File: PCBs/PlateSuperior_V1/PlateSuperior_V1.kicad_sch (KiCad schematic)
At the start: 48 parts, among them J1 Conn_01x04, J2 Conn_01x04, J3 Conn_02x10_Counter_Clockwise, SW1 SW_Push, SW10 SW_Push, SW11 SW_Push, SW12 SW_Push, SW13 SW_Push, SW14 SW_Push, SW15 SW_Push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

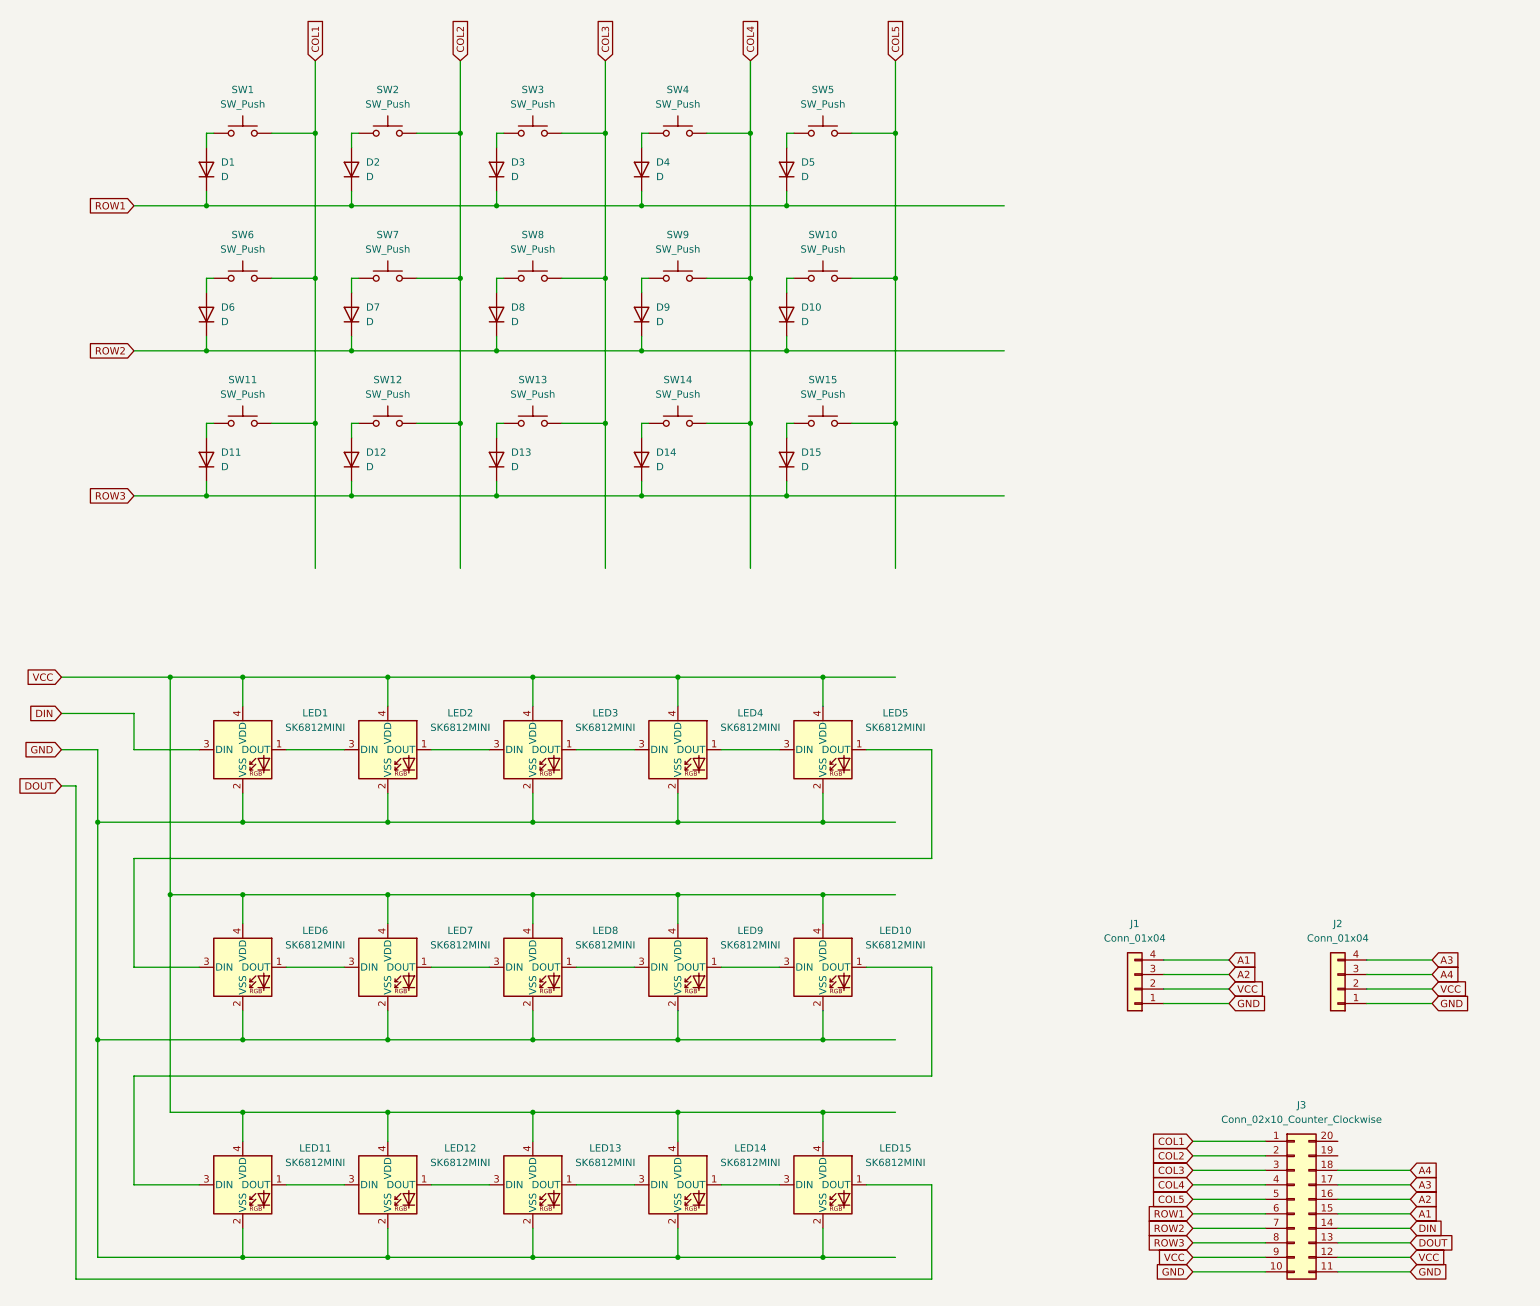
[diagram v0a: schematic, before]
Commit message: Add plates
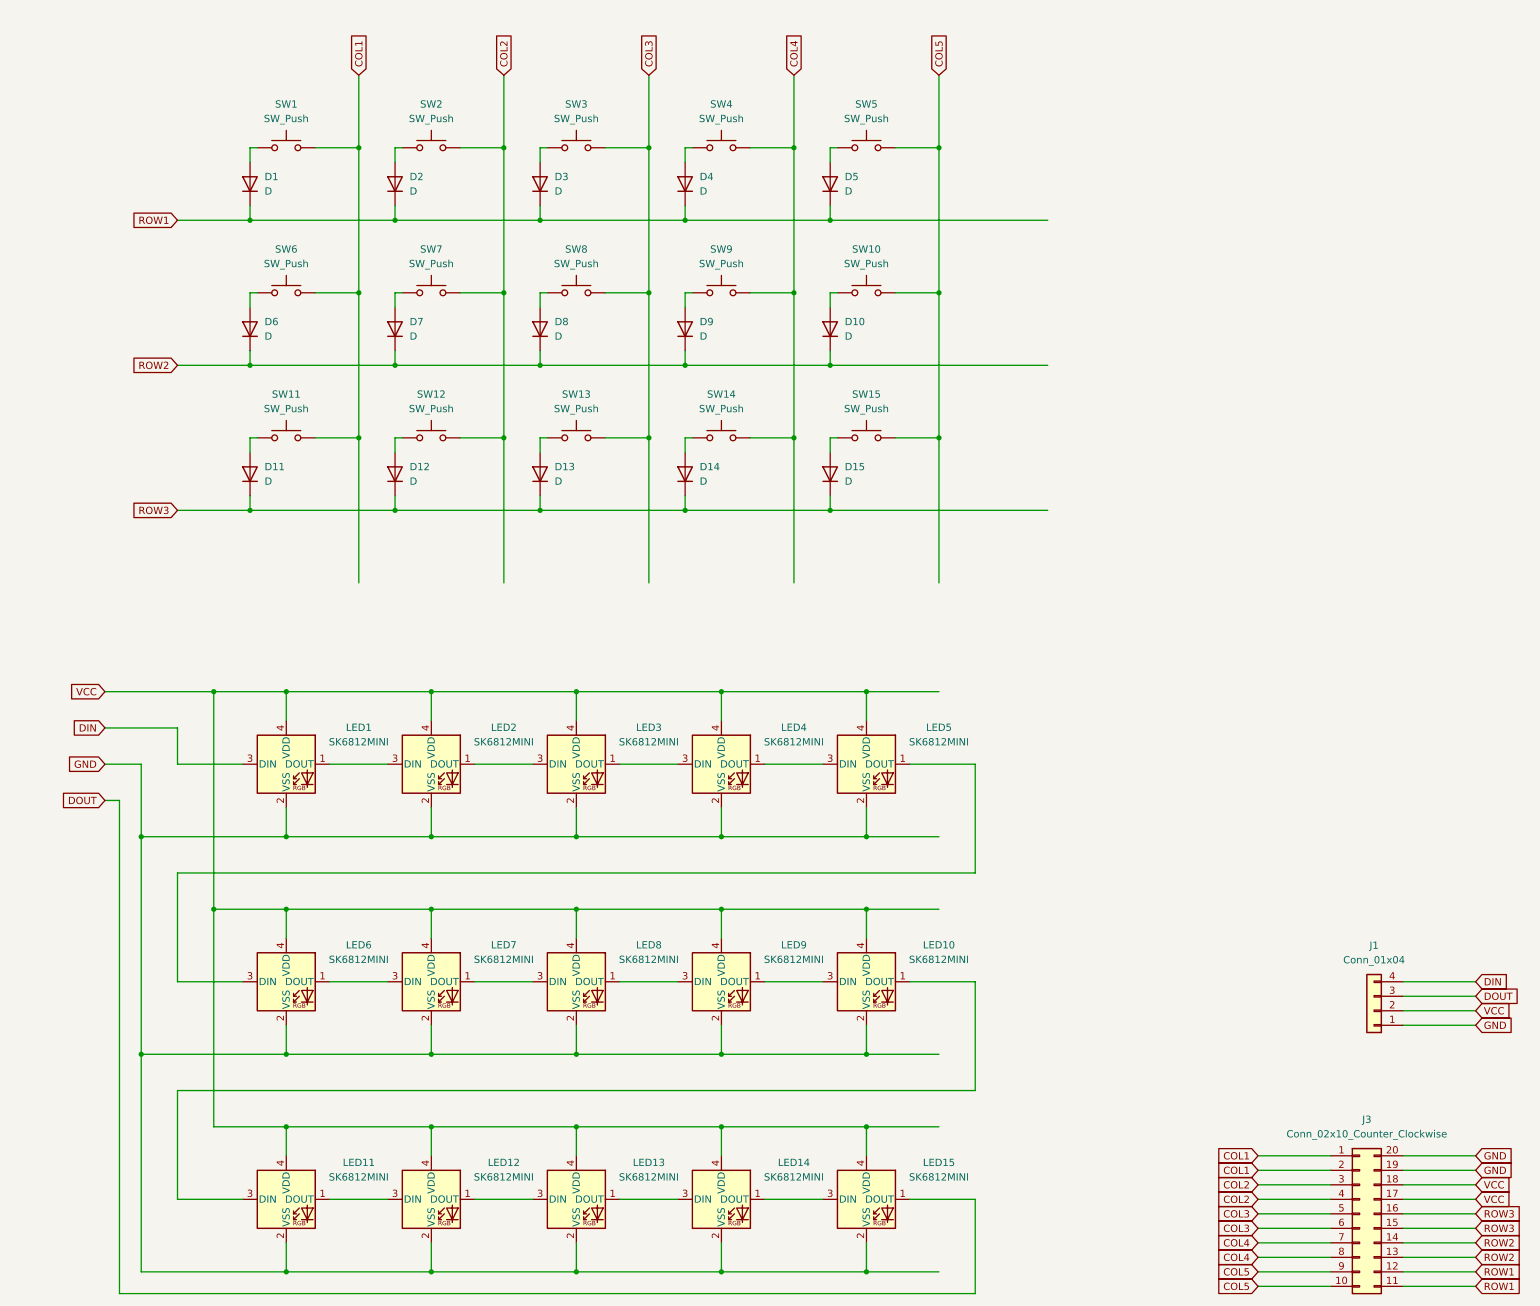
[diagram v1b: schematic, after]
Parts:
- removed J2: Conn_01x04, symbol Connector_Generic:Conn_01x04
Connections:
- net A3 is gone; now on net VCC: J3.17 (Pin_17)
- net A4 is gone; now on net VCC: J3.18 (Pin_18)
- net COL1: now also J3.2 (Pin_2)
- net COL2: now also J3.3 (Pin_3), J3.4 (Pin_4); no longer J3.2 (Pin_2)
- net COL3: now also J3.5 (Pin_5), J3.6 (Pin_6); no longer J3.3 (Pin_3)
- net COL4: now also J3.7 (Pin_7), J3.8 (Pin_8); no longer J3.4 (Pin_4)
- net COL5: now also J3.10 (Pin_10), J3.9 (Pin_9); no longer J3.5 (Pin_5)
- net DIN: now also J1.4 (Pin_4); no longer J3.14 (Pin_14)
- net DOUT: now also J1.3 (Pin_3); no longer J3.13 (Pin_13)
- net GND: now also J3.19 (Pin_19), J3.20 (Pin_20); no longer J3.10 (Pin_10), J3.11 (Pin_11)
- net ROW1: now also J3.11 (Pin_11), J3.12 (Pin_12); no longer J3.6 (Pin_6)
- net ROW2: now also J3.13 (Pin_13), J3.14 (Pin_14); no longer J3.7 (Pin_7)
- net ROW3: now also J3.15 (Pin_15), J3.16 (Pin_16); no longer J3.8 (Pin_8)
- net VCC: no longer J3.12 (Pin_12), J3.9 (Pin_9)
- removed net A1: J1.4 (Pin_4), J3.15 (Pin_15)
- removed net A2: J1.3 (Pin_3), J3.16 (Pin_16)
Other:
- moved on the sheet: D1, D10, D11, D12, D13, D14, D15, D2, D3, D4, D5, D6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
